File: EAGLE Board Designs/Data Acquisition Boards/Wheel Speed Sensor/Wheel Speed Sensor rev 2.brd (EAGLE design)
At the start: 50.8 x 56.8 mm, 20 parts, among them X1 Sensor 1, X2 Sensor 2, X4 CONNECTOR-4, X5 CONNECTOR-4

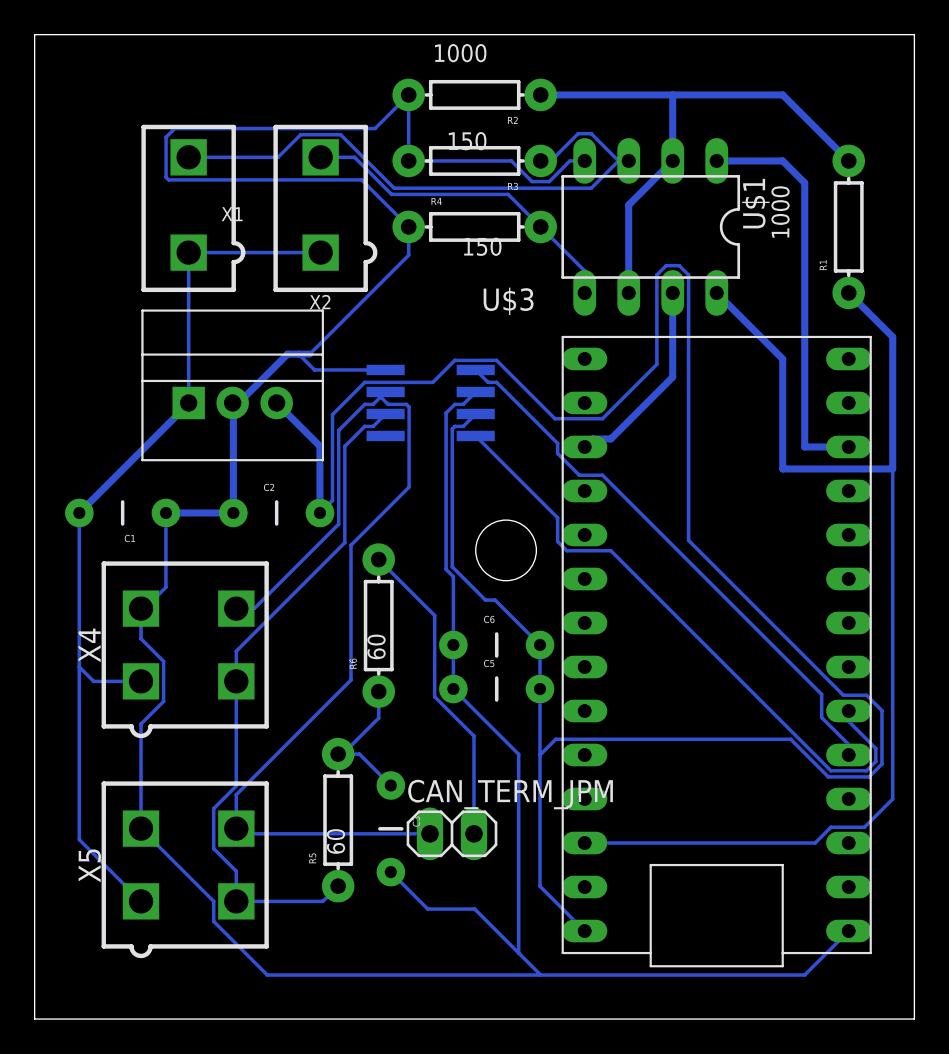
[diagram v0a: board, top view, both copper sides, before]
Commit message: Updated to work with Electronics Lab DRC
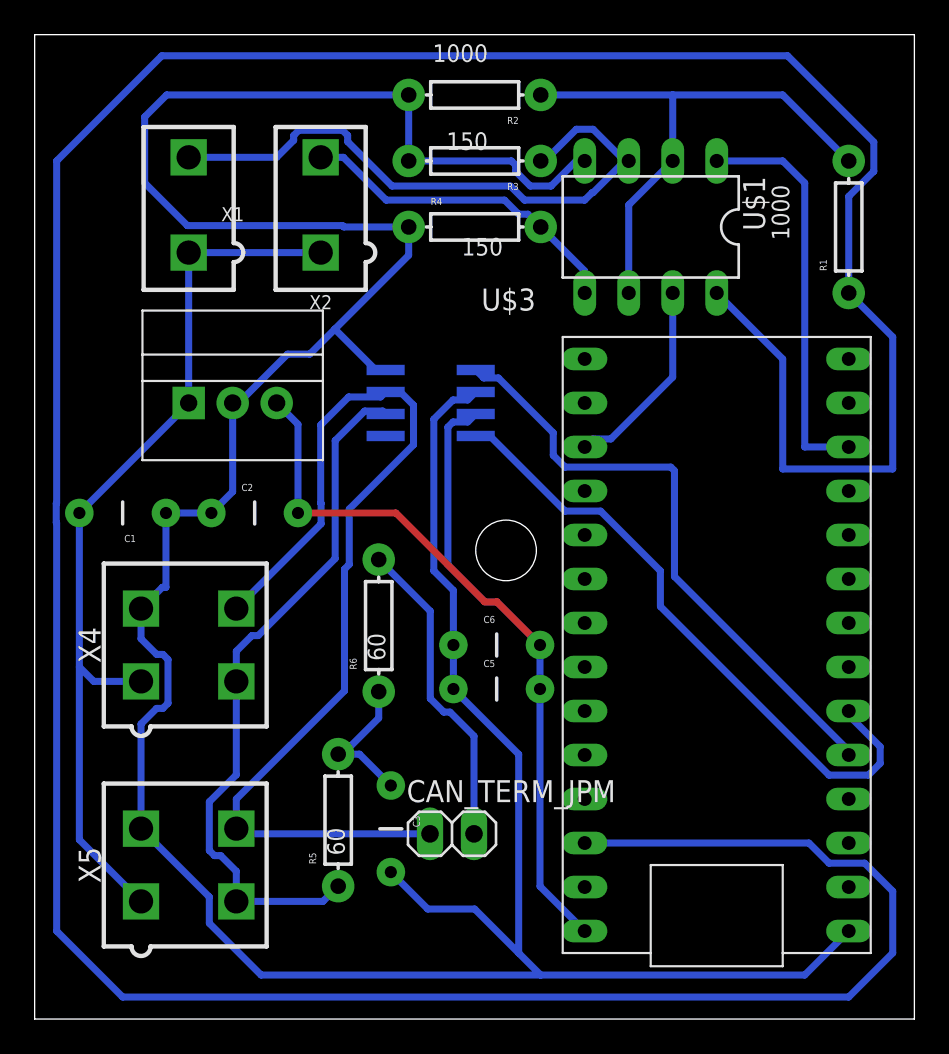
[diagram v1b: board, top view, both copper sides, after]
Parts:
- moved C2 1.27 mm to (-16.5, 10.2)
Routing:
- net 3.3V: track 67.2 -> 208.2 mm
- net +5V: track 132.7 -> 58.7 mm
- net GND: track 190.8 -> 193.9 mm
- net TX: track 32.2 -> 35.2 mm
- net N$4: track 33.7 -> 35.4 mm
- net CANL: track 39.3 -> 40.6 mm
- net RX: track 35.7 -> 36.7 mm
